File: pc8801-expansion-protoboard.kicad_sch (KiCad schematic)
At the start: 40 parts, among them J1 Solder Side, J2 Parts Side, J3 5V, J4 12V, J5 -12V, J6 GND_1, J7 GND_2, SW1 Reset ESP, U1 ExpansionEdge, U10 74LS165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

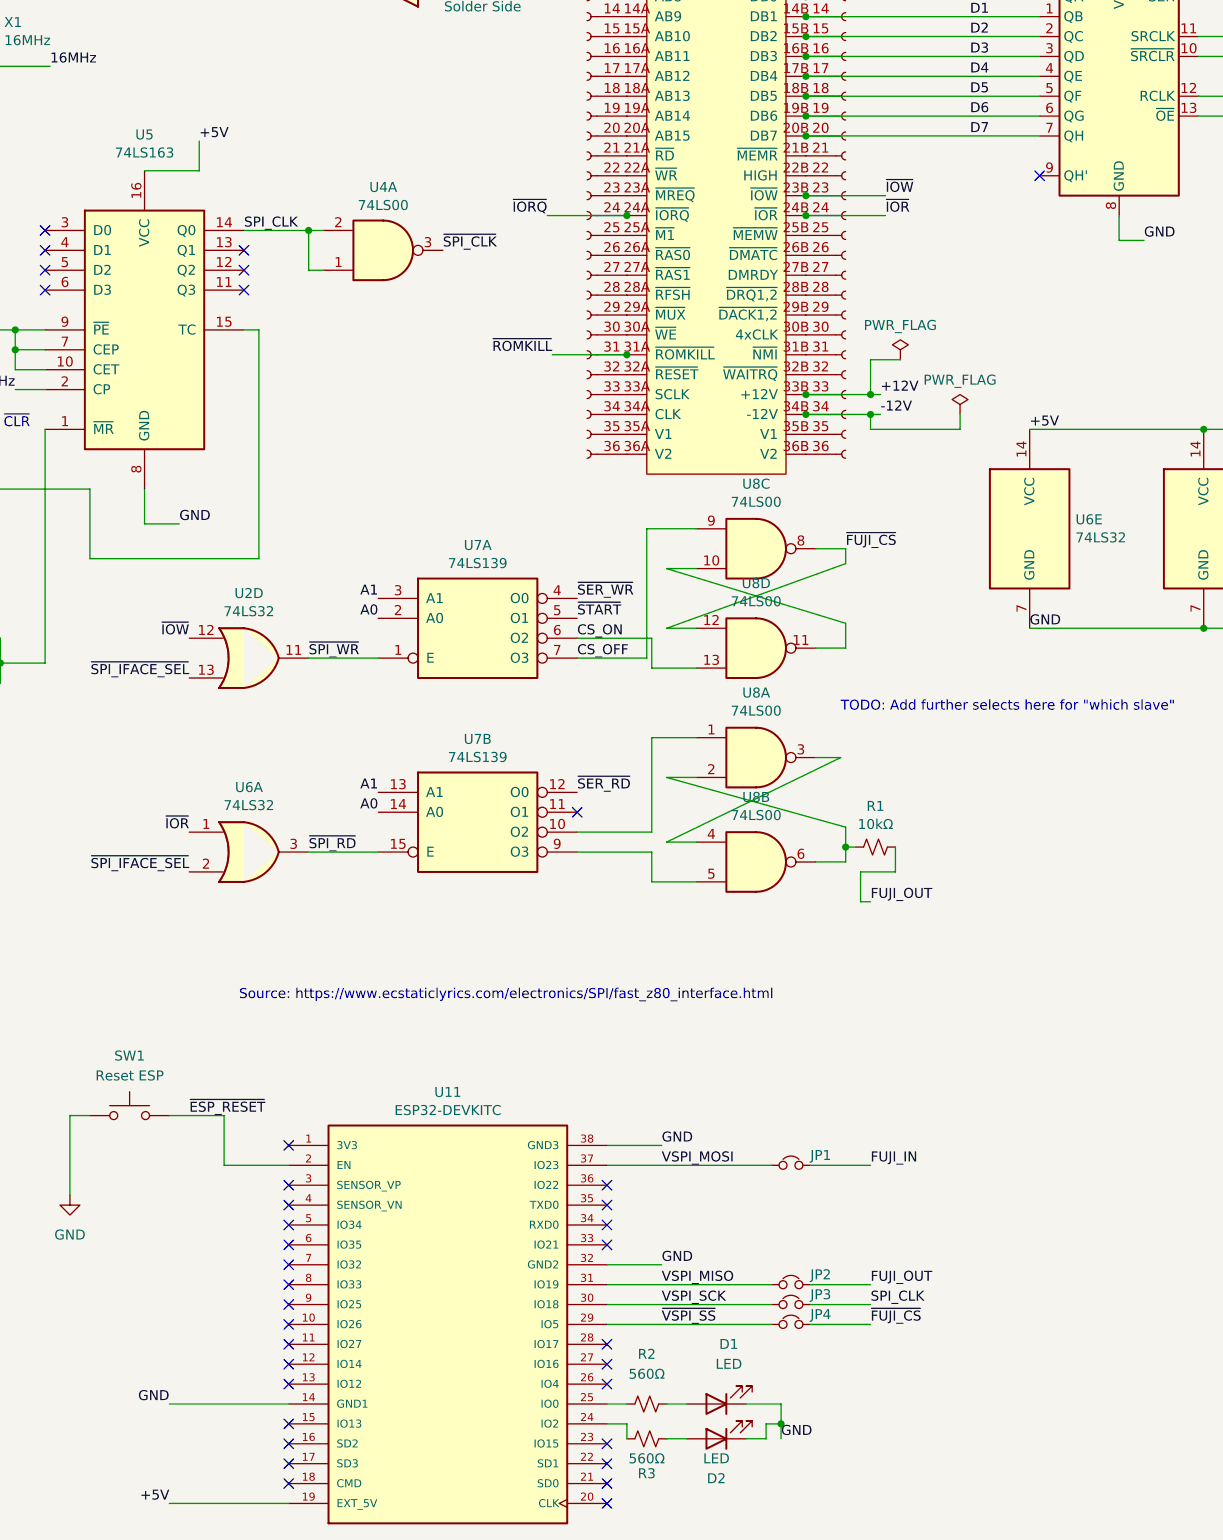
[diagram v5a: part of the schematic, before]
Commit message: Add bypass caps for counter and ESP
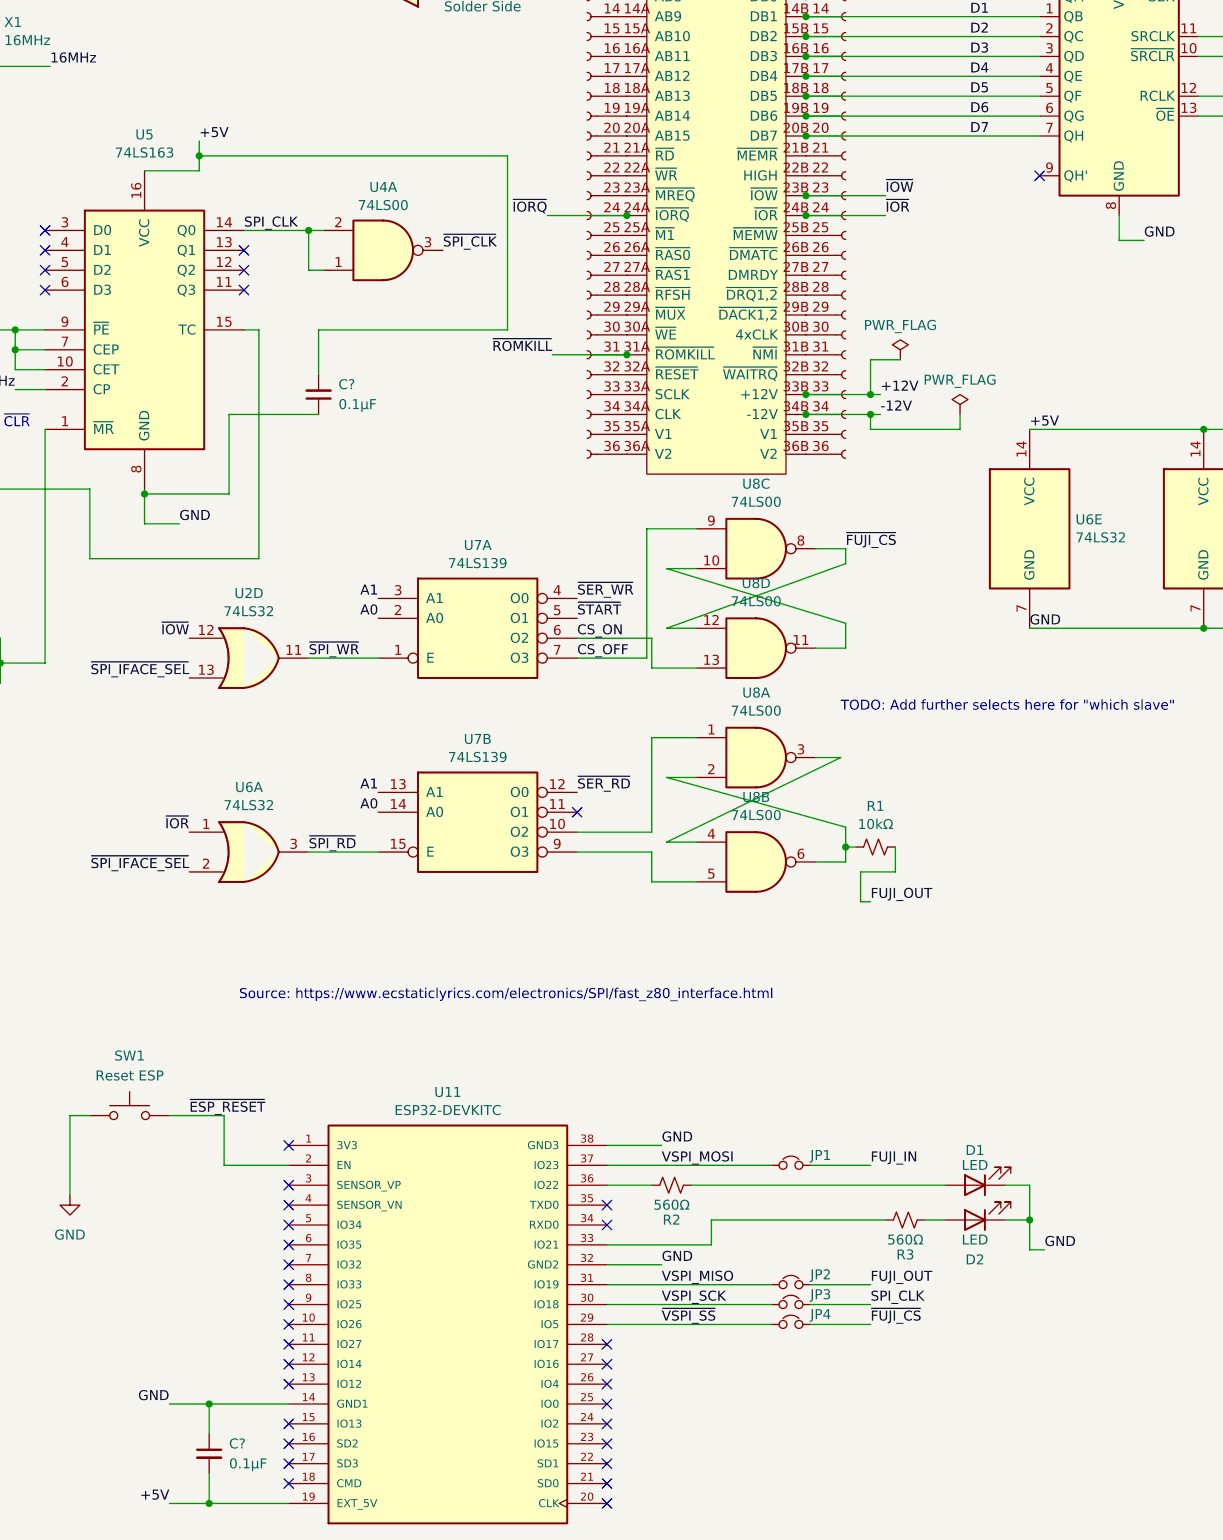
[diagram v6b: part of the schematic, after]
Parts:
- added C? (x2): 0.1µF, Capacitor_THT:C_Disc_D5.0mm_W2.5mm_P2.50mm, symbol Device:C_Small
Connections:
- net +5V: now also C?.2, C?.2
- net GND: now also C?.1, C?.1
- net at U11.24 (IO2): no longer R3.1
- net at U11.25 (IO0): no longer R2.1
- net at U11.33 (IO21): now also R3.1
- net at U11.36 (IO22): now also R2.1
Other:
- moved on the sheet: D1, D2, R2, R3
